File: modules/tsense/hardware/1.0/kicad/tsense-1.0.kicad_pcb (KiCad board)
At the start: 2 copper layers, 75 x 75 mm, 36 parts, among them J1 T0, J2 T1, J3 T2, J4 T3, J5 T4, J6 T5, J7 T6, J8 T7, J9 CAN, SW1 SCR, SW2 INSTANCE, SW3 PRG, U1 Teensy_3.2, U2 MCP2551-I-P, U3 TMR1-1211

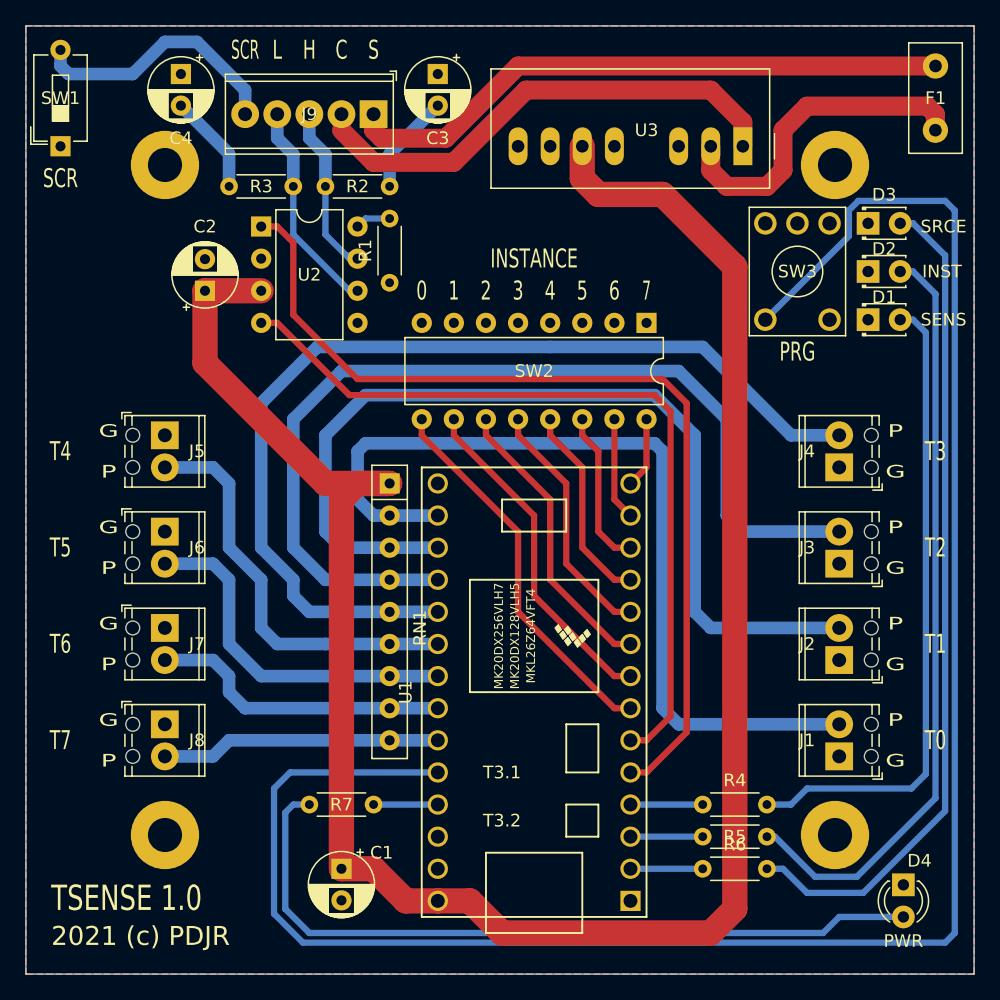
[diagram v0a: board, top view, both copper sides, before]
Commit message: Add installer preferred connectors
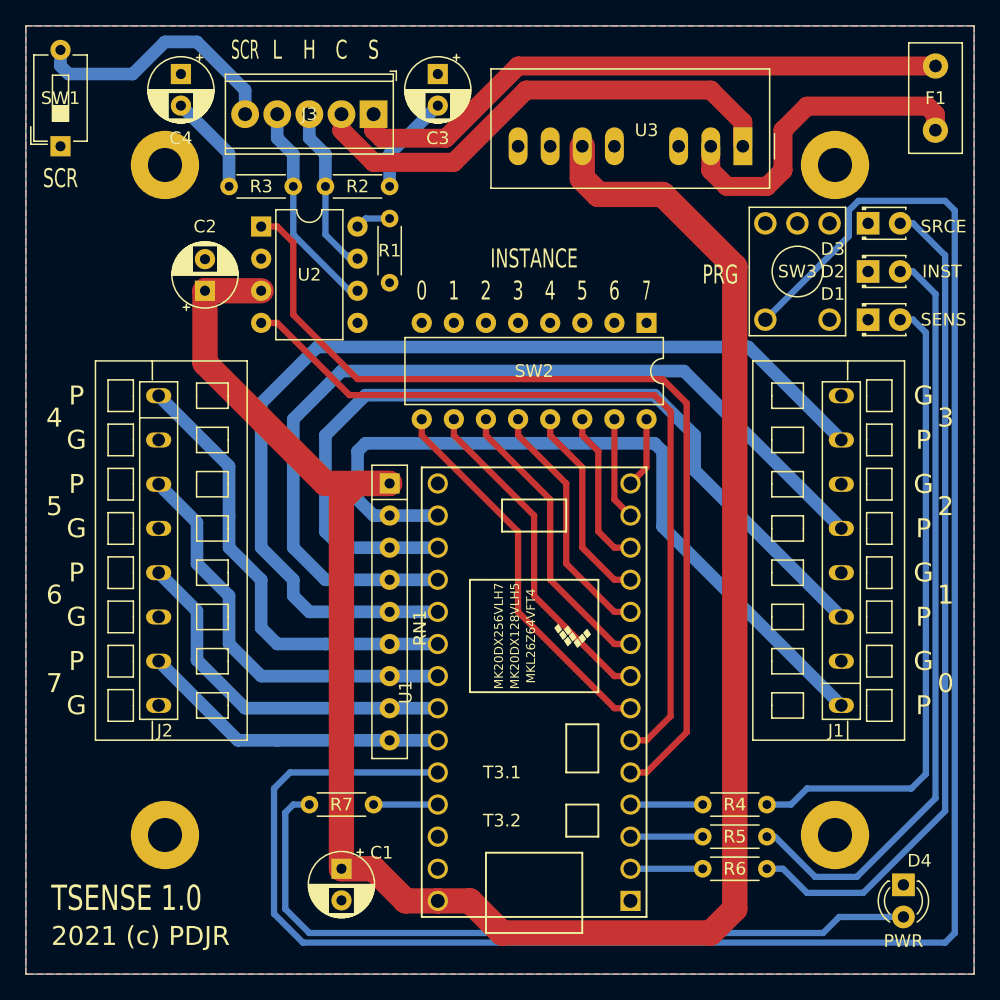
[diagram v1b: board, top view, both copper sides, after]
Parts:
- removed the J3 at (200.3, 129.5)
- removed J4: T3, TerminalBlock_Phoenix:TerminalBlock_Phoenix_MPT-0,5-2-2.54_1x02_P2.54mm_Horizontal
- removed J5: T4, TerminalBlock_Phoenix:TerminalBlock_Phoenix_MPT-0,5-2-2.54_1x02_P2.54mm_Horizontal
- removed J6: T5, TerminalBlock_Phoenix:TerminalBlock_Phoenix_MPT-0,5-2-2.54_1x02_P2.54mm_Horizontal
- removed J7: T6, TerminalBlock_Phoenix:TerminalBlock_Phoenix_MPT-0,5-2-2.54_1x02_P2.54mm_Horizontal
- removed J8: T7, TerminalBlock_Phoenix:TerminalBlock_Phoenix_MPT-0,5-2-2.54_1x02_P2.54mm_Horizontal
- J1: value T0 -> Screw_Terminal_01x08; footprint TerminalBlock_Phoenix:TerminalBlock_Phoenix_MPT-0,5-2-2.54_1x02_P2.54mm_Horizontal -> PDJR:WAGO-250-108
- J2: value T1 -> Screw_Terminal_01x08; footprint TerminalBlock_Phoenix:TerminalBlock_Phoenix_MPT-0,5-2-2.54_1x02_P2.54mm_Horizontal -> PDJR:WAGO-250-108
- moved J2 56.0 mm to (146.0, 123.5), turned to 270 degrees
- moved J1 11.3 mm to (201.0, 133.5)
- renumbered J9 to J3
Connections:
- J1 pad 1: GND -> /SENSOR_T0
- J1 pad 2: /SENSOR_T0 -> GND
- J2 pad 1: GND -> /SENSOR_T4
- J2 pad 2: /SENSOR_T1 -> GND
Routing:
- net /SENSOR_T0: track 70.2 -> 61.3 mm
- net /SENSOR_T1: track 74.8 -> 68.1 mm
- net /SENSOR_T6: track 23.9 -> 28.8 mm
- net /SENSOR_T2: track 77.1 -> 72.7 mm
- net /SENSOR_T5: track 28.2 -> 32.5 mm
- net /SENSOR_T4: track 32.6 -> 36.2 mm
- net /SENSOR_T7: track 22.1 -> 24.7 mm
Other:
- board text added: "G"
- board text added: "P"
- board text removed: "G P"
- board text removed: "P G"
